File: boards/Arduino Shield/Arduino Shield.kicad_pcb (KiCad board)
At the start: 2 copper layers, 114.3 x 76.2 mm, 21 parts, among them J1 Screw_Terminal_01x07, J11 Screw_Terminal_01x08, J2 Screw_Terminal_01x08, J3 Screw_Terminal_01x08, J4 Screw_Terminal_01x08, J5 Screw_Terminal_01x08, J6 Screw_Terminal_01x08, J7 Screw_Terminal_01x08, J8 Screw_Terminal_01x07, J9 Screw_Terminal_01x10, U1 A000062

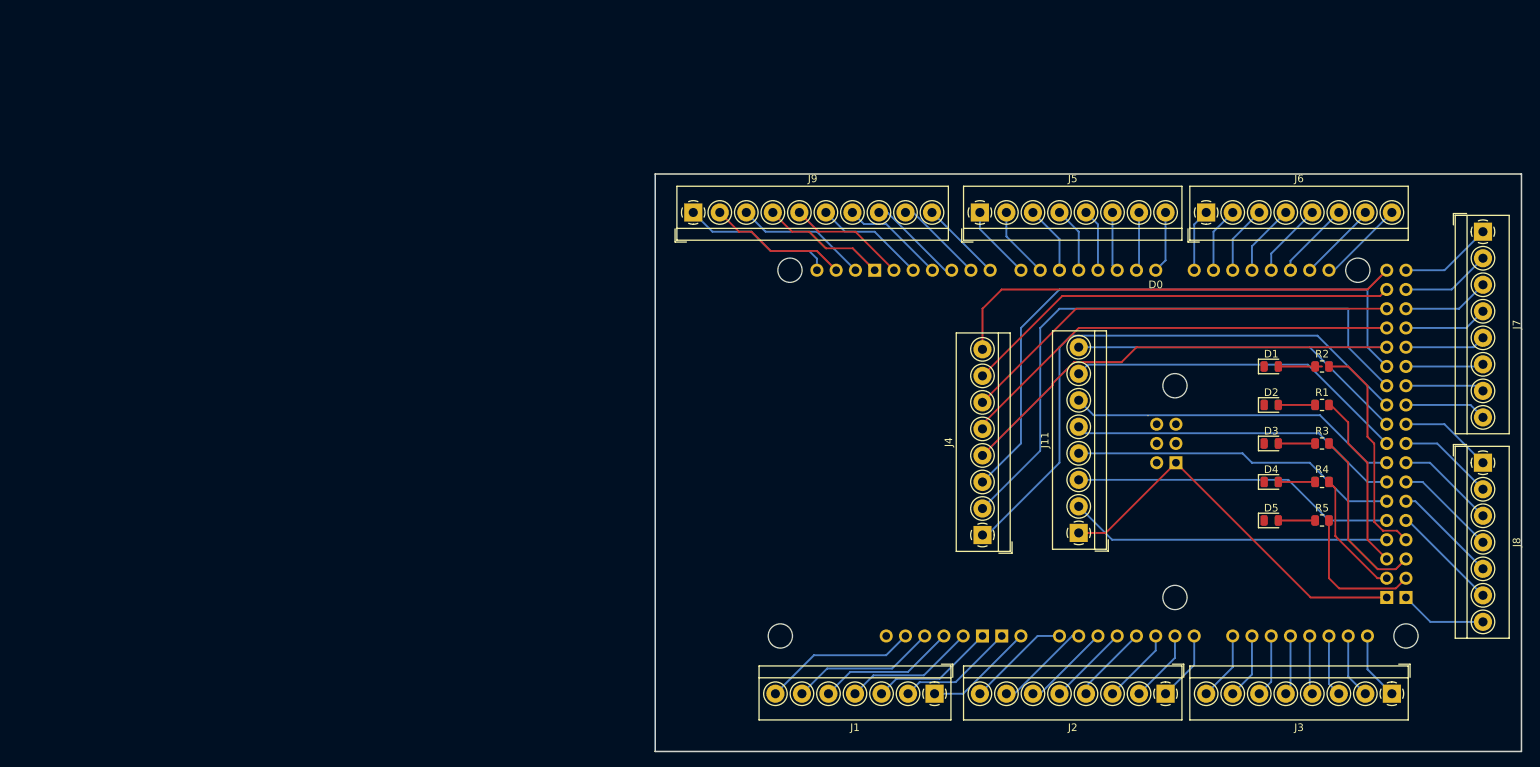
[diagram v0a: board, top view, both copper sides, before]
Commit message: Add filled zone and minor corrections
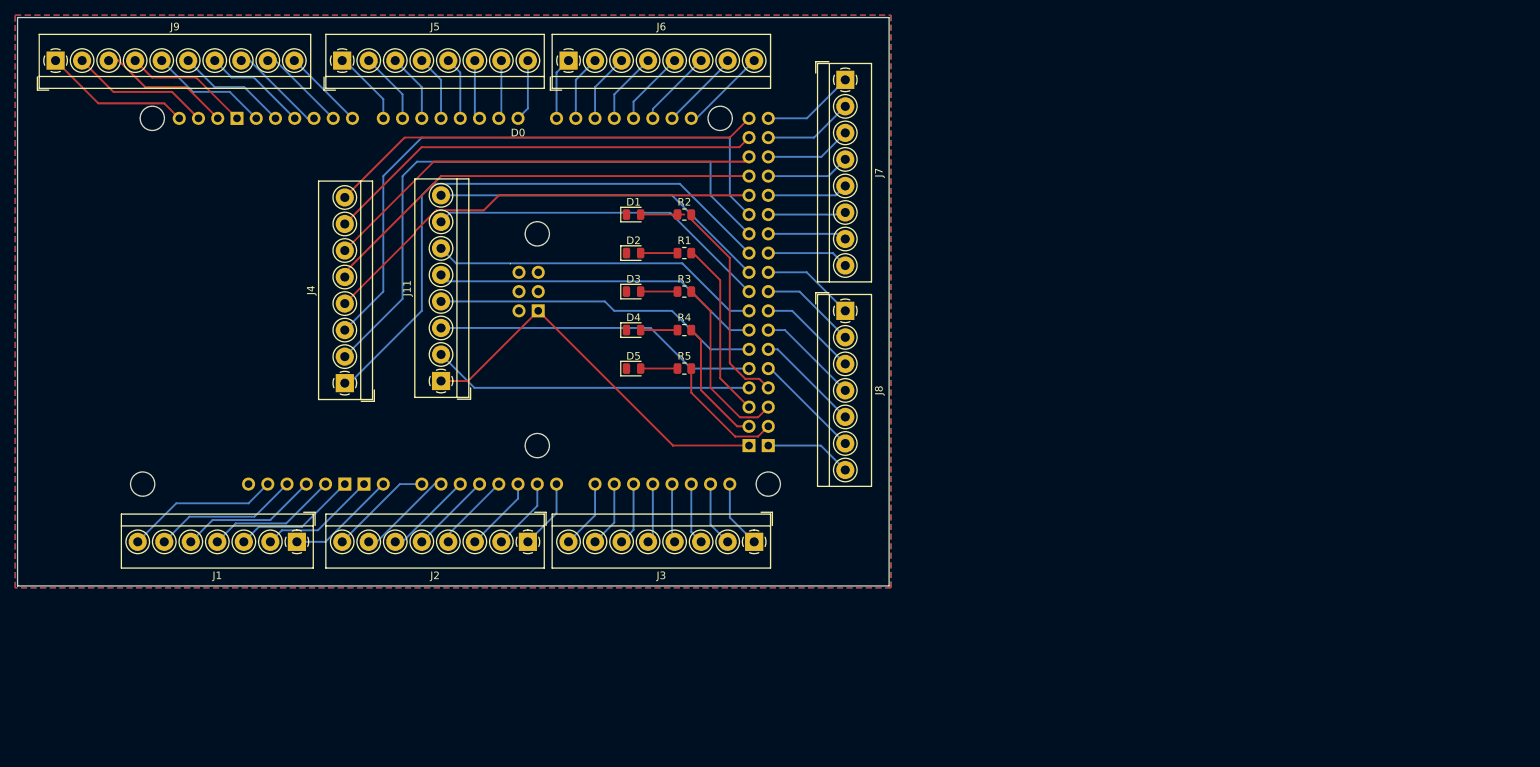
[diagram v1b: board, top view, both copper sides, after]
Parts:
- moved J11 86.5 mm to (75.9, 68.0)
- moved J7 86.5 mm to (129.2, 28.2)
- moved J8 86.5 mm to (129.2, 58.7)
- moved U1 86.5 mm to (22.5, 84.1)
- moved J1 86.5 mm to (56.9, 89.2)
- moved J3 86.5 mm to (117.2, 89.2)
- moved J6 86.5 mm to (92.7, 25.7)
- moved J9 86.5 mm to (25.0, 25.7)
- moved R1 86.5 mm to (108.0, 51.1)
- moved R2 86.5 mm to (108.0, 46.0)
- moved R3 86.5 mm to (108.0, 56.2)
- moved R4 86.5 mm to (108.0, 61.2)
- moved R5 86.5 mm to (108.0, 66.3)
- moved D1 86.5 mm to (101.3, 46.0)
- moved D2 86.5 mm to (101.3, 51.1)
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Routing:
- net Net-(J4-Pin_8): track 60.8 -> 57.7 mm
- net Net-(U1-D53): track 18.9 -> 16.3 mm
- net Net-(U1-D49): track 29.6 -> 28.1 mm
- net Net-(J4-Pin_2): track 80.9 -> 80.0 mm
- net Net-(J9-Pin_1): track 20.4 -> 19.5 mm
- added copper zone on B.Cu, net GND
- added copper zone on F.Cu, net GND
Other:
- board size 114.3 x 76.2 mm -> 115 x 75 mm
- board text removed: "- 3.0 inches -"
- board text removed: "- 4.5 inches -"

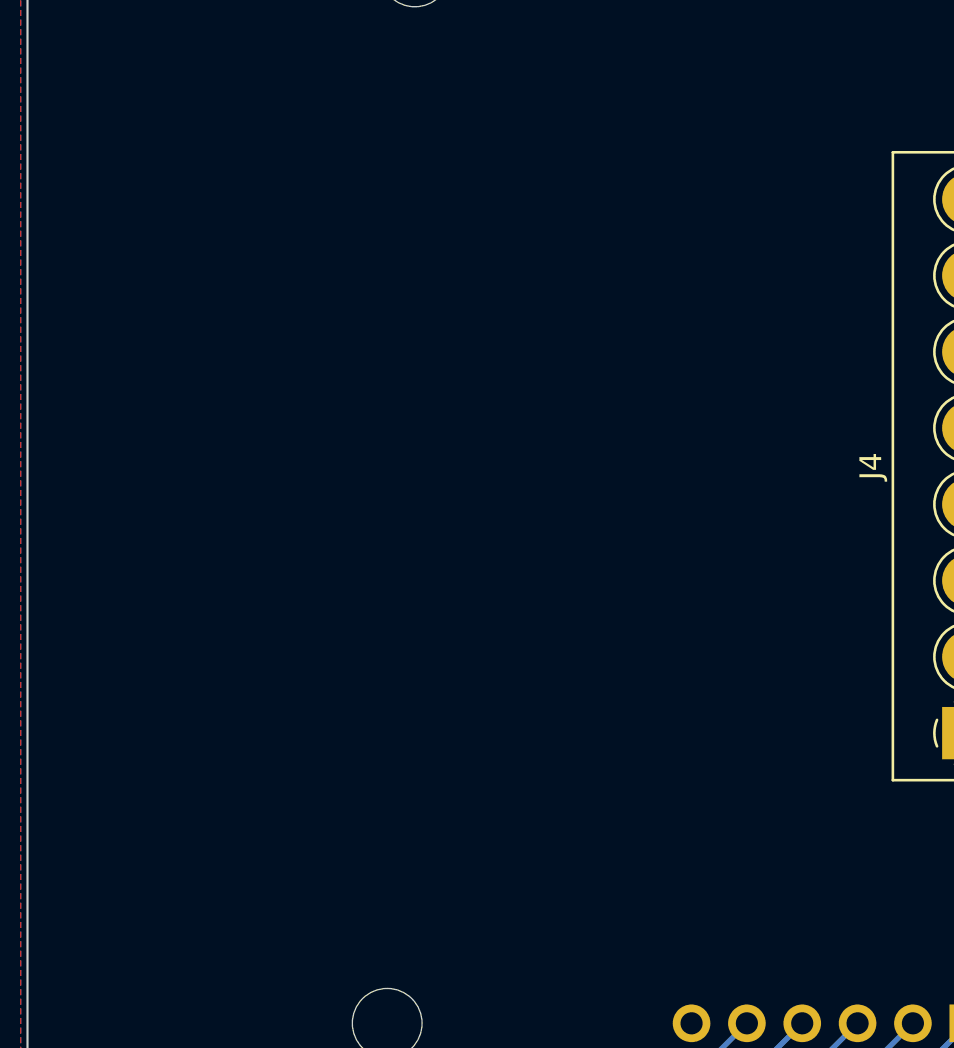
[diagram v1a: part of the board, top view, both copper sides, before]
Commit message: added hole and logo and names
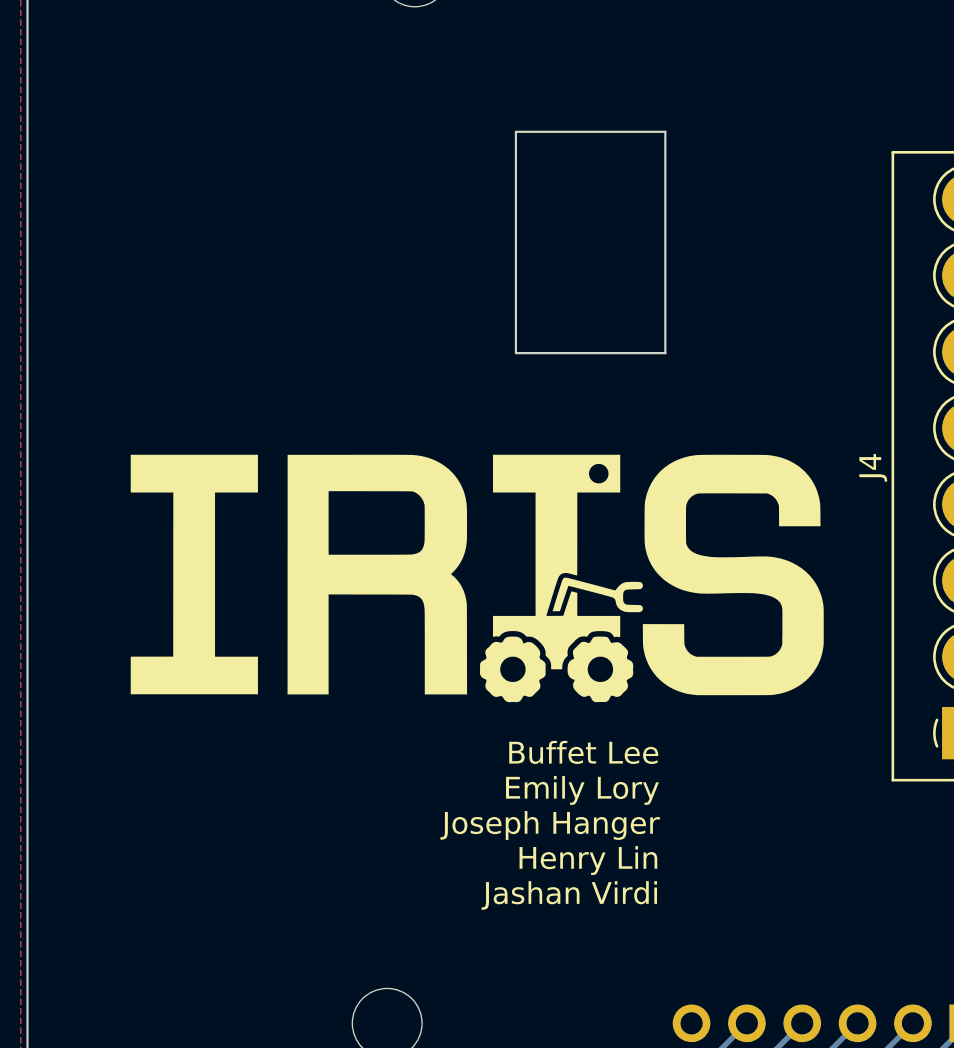
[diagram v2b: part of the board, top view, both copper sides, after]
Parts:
- added G***: LOGO, Custom_Silkscreen_and_memes:irislogo, F.Cu at (40.6, 61.0)
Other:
- outline, holes or cut-outs redrawn
- board text added: "Buffet Lee Emily Lory Joseph Hanger Henry Lin Jashan Virdi"

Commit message: Add GND
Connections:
- J1 pad 2: Net-(J1-Pin_2) -> GND
- J1 pad 3: Net-(J1-Pin_3) -> GND
- J11 pad 1: Net-(J11-Pin_1) -> GND
- J8 pad 7: Net-(J8-Pin_7) -> GND
- J9 pad 4: Net-(J9-Pin_4) -> GND
- U1 pad GND1: Net-(J1-Pin_3) -> GND
- U1 pad GND2: Net-(J1-Pin_2) -> GND
- U1 pad GND3: Net-(J9-Pin_4) -> GND
- U1 pad GND4: Net-(J11-Pin_1) -> GND
- U1 pad GND5: Net-(J8-Pin_7) -> GND
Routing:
- net GND: track 0.00 -> 111.9 mm
- net Net-(J11-Pin_1): track 51.8 -> 0.00 mm
- net Net-(J9-Pin_4): track 16.6 -> 0.00 mm
- net Net-(J1-Pin_3): track 16.5 -> 0.00 mm
- net Net-(J1-Pin_2): track 15.5 -> 0.00 mm
- net Net-(J8-Pin_7): track 11.5 -> 0.00 mm

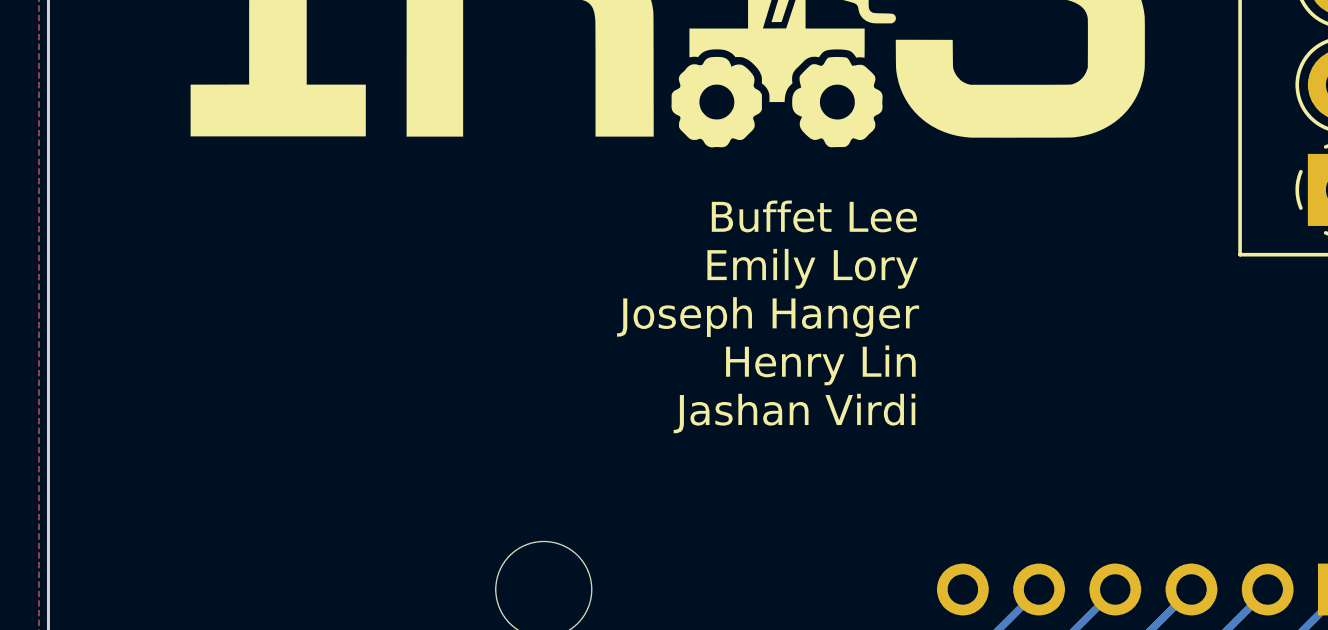
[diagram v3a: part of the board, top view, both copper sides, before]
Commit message: Added IRIS XV and Arduino Shield v4
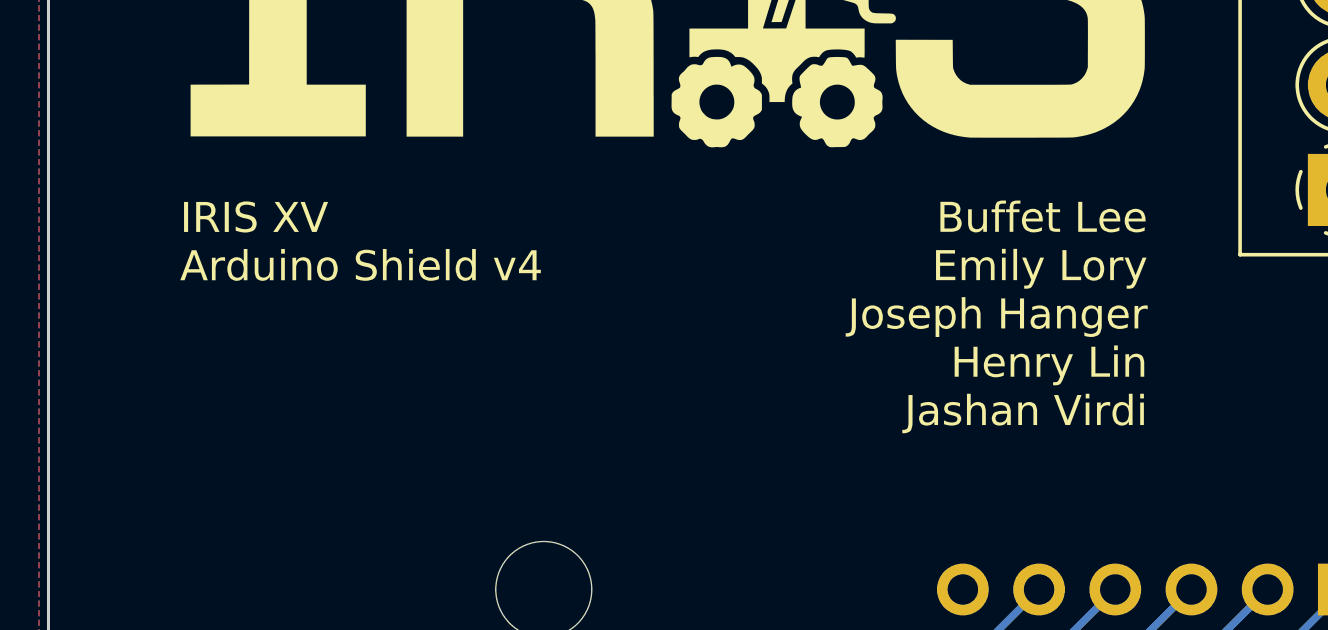
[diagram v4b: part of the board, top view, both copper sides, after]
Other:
- board text added: "IRIS XV Arduino Shield v4"
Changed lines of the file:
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@@
     (fp_arc (start 98.552 0.254) (mid 96.52 0.914237) (end 94.488 0.254)
       (stroke (width 0.15) (type solid)) (layer "B.CrtYd"))
-    (fp_arc (start 99.8728 -1.7018) (mid 99.650928 -1.077973) (end 99.314 -0.508)
+    (fp_arc (start 99.8728 -1.7018) (mid 99.650934 -1.077968) (end 99.314 -0.508)
       (stroke (width 0.15) (type solid)) (layer "B.CrtYd"))
     (fp_circle (center 13.97 -2.54) (end 17.42 -2.54)
@@
   (gr_rect (start 20 20) (end 135 95)
     (stroke (width 0.1) (type default)) (fill none) (layer "Edge.Cuts"))
-  (gr_text "Buffet Lee\nEmily Lory\nJoseph Hanger\nHenry Lin\nJashan Virdi" (at 49.022 76.2) (layer "F.SilkS")
+  (gr_text "Buffet Lee\nEmily Lory\nJoseph Hanger\nHenry Lin\nJashan Virdi" (at 56.642 76.2) (layer "F.SilkS")
     (effects (font (size 1 1) (thickness 0.15)) (justify right bottom))
   )
+  (gr_text "IRIS XV\nArduino Shield v4" (at 24.384 71.374) (layer "F.SilkS")
+    (effects (font (size 1 1) (thickness 0.15)) (justify left bottom))
+  )
   (segment (start 56.86 89.18) (end 60.64 89.18) (width 0.25) (layer "B.Cu") (net 1))

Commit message: Aesthetics
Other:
- board text added: "IRIS XV Arduino Shield Ver.4"
- board text removed: "IRIS XV Arduino Shield v4"
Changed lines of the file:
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@@
     (fp_arc (start 98.552 0.254) (mid 96.52 0.914237) (end 94.488 0.254)
       (stroke (width 0.15) (type solid)) (layer "B.CrtYd"))
-    (fp_arc (start 99.8728 -1.7018) (mid 99.650934 -1.077968) (end 99.314 -0.508)
+    (fp_arc (start 99.8728 -1.7018) (mid 99.650928 -1.077973) (end 99.314 -0.508)
       (stroke (width 0.15) (type solid)) (layer "B.CrtYd"))
     (fp_circle (center 13.97 -2.54) (end 17.42 -2.54)
@@
     (effects (font (size 1 1) (thickness 0.15)) (justify right bottom))
   )
-  (gr_text "IRIS XV\nArduino Shield v4" (at 24.384 71.374) (layer "F.SilkS")
+  (gr_text "IRIS XV\nArduino Shield Ver.4" (at 24.384 71.374) (layer "F.SilkS")
     (effects (font (size 1 1) (thickness 0.15)) (justify left bottom))
   )

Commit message: Add labeling
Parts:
- moved D5 4.34 mm to (101.3, 62.0)
- moved R5 4.34 mm to (108.0, 62.0)
- moved D4 3.07 mm to (101.3, 58.2)
- moved R4 3.07 mm to (108.0, 58.2)
- moved D3 2.06 mm to (101.3, 54.1)
- moved R3 2.06 mm to (108.0, 54.1)
- moved J9 1.58 mm to (25.3, 24.1)
- moved J5 1.58 mm to (63.2, 24.1)
- moved J6 1.58 mm to (93.0, 24.1)
- moved J1 1.51 mm to (57.0, 90.7)
- moved J2 1.50 mm to (87.4, 90.7)
- moved J3 1.50 mm to (117.3, 90.7)
- moved J8 1.47 mm to (130.7, 58.5)
- moved J7 1.47 mm to (130.7, 28.1)
- moved D2 0.79 mm to (101.2, 50.3)
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- renumbered R2 to R1, R1 to R2
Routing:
- net GND: track 111.9 -> 106.9 mm
- net Net-(U1-D53): track 16.3 -> 20.5 mm
- net Net-(U1-D52): track 16.8 -> 19.6 mm
- net Net-(J6-Pin_8): track 11.5 -> 13.4 mm
- net Net-(U1-D51): track 23.5 -> 25.3 mm
- net Net-(J6-Pin_7): track 10.7 -> 12.4 mm
- net Net-(J6-Pin_6): track 10.3 -> 11.9 mm
- net Net-(J6-Pin_5): track 9.87 -> 11.5 mm
- net Net-(J6-Pin_2): track 8.67 -> 10.4 mm
- net Net-(J6-Pin_1): track 8.27 -> 9.96 mm
- net Net-(J5-Pin_7): track 7.76 -> 9.44 mm
- net Net-(J6-Pin_4): track 9.47 -> 11.1 mm
- net Net-(J6-Pin_3): track 9.07 -> 10.8 mm
- net Net-(J5-Pin_8): track 8.16 -> 9.84 mm
- net Net-(J8-Pin_6): track 14.3 -> 15.9 mm
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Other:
- board text added: "3.3V"
- board text added: "5V"
- board text added: "A0"
- board text added: "A1"
- board text added: "A10"
- board text added: "A11"
- board text added: "A2"
- board text added: "A3"
- board text added: "A4"
- board text added: "A5"
- board text added: "A6"
- board text added: "A7"
- board text added: "A8"
- board text added: "A9"
- board text added: "AREF"
- board text added: "CANRX"
- board text added: "CANTX"
- board text added: "D10"
- board text added: "D11"
- board text added: "D12"
- board text added: "D13"
- board text added: "D2"
- board text added: "D20"
- board text added: "D22"
- board text added: "D23"
- board text added: "D24"
- board text added: "D25"
- board text added: "D26"
- board text added: "D27"
- board text added: "D28"
- board text added: "D29"
- board text added: "D3"
- board text added: "D30"
- board text added: "D31"
- board text added: "D32"
- board text added: "D33"
- board text added: "D34"
- board text added: "D35"
- board text added: "D36"
- board text added: "D37"
- board text added: "D38"
- board text added: "D39"
- board text added: "D4"
- board text added: "D40"
- board text added: "D41"
- board text added: "D42"
- board text added: "D43"
- board text added: "D44"
- board text added: "D45"
- board text added: "D46"
- board text added: "D47"
- board text added: "D48"
- board text added: "D5"
- board text added: "D6"
- board text added: "D7"
- board text added: "D8"
- board text added: "D9"
- board text added: "DAC1"
- board text added: "DAC2"
- board text added: "GND"
- board text added: "IOREF"
- board text added: "JLCJLCJLCJLC"
- board text added: "RESET"
- board text added: "RX0"
- board text added: "RX1"
- board text added: "RX2"
- board text added: "RX3"
- board text added: "SCL"
- board text added: "SCL1"
- board text added: "SDA"
- board text added: "SDA1"
- board text added: "TX0"
- board text added: "TX1"
- board text added: "TX2"
- board text added: "TX3"
- board text added: "Vin"
